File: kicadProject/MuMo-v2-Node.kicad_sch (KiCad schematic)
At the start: 76 parts, among them Q1 PJC7400, SW1 Boot0, SW2 Reset, U1 MCP73123, U2 LoRa-E5, U3 CP2102N, U4 eInk_Display_1.54"200x200px, U5 BME680, U6 TSL25911, U7 BR24G512FVT-5AE2

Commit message: V2.1
Minor update, fixing issues #2 #3 #6 #7 #8 #9 #10 #11 #12 #13 #14 #15 #16 #17 #18 and #19
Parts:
- removed R6: 470, thisProjectLibrary:0603_1608Metric, symbol Device:R
- removed SW1: Boot0, thisProjectLibrary:SW_SPST_PTS815, symbol Switch:SW_Push
- removed TP1, TP2, TP3: GND, TestPoint:TestPoint_THTPad_1.5x1.5mm_Drill0.7mm, symbol Connector:TestPoint_Probe
- removed TP5: GND, TestPoint:TestPoint_THTPad_2.5x2.5mm_Drill1.2mm, symbol Connector:TestPoint_Probe
- added C28: 4u7, thisProjectLibrary:0603_1608Metric, symbol Device:C
- added C29: 100n, thisProjectLibrary:0603_1608Metric, symbol Device:C
- added C30: 1uF/50V, thisProjectLibrary:0603_1608Metric, symbol Device:C_Small
- added JP1: Cut to disable charging, Jumper:SolderJumper-2_P1.3mm_Bridged2Bar_Pad1.0x1.5mm, symbol Jumper:SolderJumper_2_Bridged
- added U8: BR24G512FVT-5AE2, thisProjectLibrary:TSSOP-B8, symbol thisProjectLibrary:BR24G512FVT
- C15: value 1uF/50V -> 1uF/25V
- C17: value 4u7 -> 100n
- C23, C25: value 100n -> 4u7
- CONN1: value SWD -> DEBUG-SWD; footprint Connector_PinHeader_2.54mm:PinHeader_1x03_P2.54mm_Vertical -> Connector_PinHeader_2.54mm:PinHeader_1x05_P2.54mm_Vertical; symbol Connector:Conn_01x03_Male -> Connector:Conn_01x05_Male
- CONN6: value UART -> UART1
- R10, R11, R12: value 3K3 -> 5K1
- TP4, TP6: footprint TestPoint:TestPoint_THTPad_2.5x2.5mm_Drill1.2mm -> TestPoint:TestPoint_THTPad_1.5x1.5mm_Drill0.7mm
- TP7: value TestPoint_Probe -> 5V; footprint TestPoint:TestPoint_THTPad_2.5x2.5mm_Drill1.2mm -> TestPoint:TestPoint_THTPad_1.5x1.5mm_Drill0.7mm
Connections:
- net +5V: now also D4.4; no longer D4.2
- net D+: now also D4.2; no longer D4.3
- net D-: now also D4.3; no longer D4.4
- net GND: now also CONN1.2 (Pin_2), C28.2, C29.2, C30.1, U8.2 (A1), U8.3 (A3), U8.4 (GND); no longer CONN1.1 (Pin_1)
- net SWCLK: now also CONN1.4 (Pin_4); no longer CONN1.3 (Pin_3)
- net SWDIO: now also CONN1.3 (Pin_3); no longer CONN1.2 (Pin_2)
- net PREVGL: now reaches C14.2, CONN3.23 (Pin_23), D2.2 (A)
- net GATE-DRIVE: now reaches CONN3.2 (Pin_2), Q1.1 (G), R9.2
- net VSH: now reaches C10.2, CONN3.20 (Pin_20)
- net PREVGH: now reaches C13.2, CONN3.21 (Pin_21), D3.1 (K)
- net VSL: now reaches C11.2, CONN3.22 (Pin_22)
- net VCOM: now reaches C15.2, CONN3.24 (Pin_24)
- net CURRENT-SENSE: now reaches CONN3.3 (Pin_3), Q1.2 (S), R8.1
- net VGL: now reaches CONN3.4 (Pin_4)
- net VGL: now also C30.2
- net VGH: now reaches C8.2, CONN3.5 (Pin_5)
- net UART1-TX: now reaches U2.10 (PB6)
- net UART1-TX: now also CONN6.2; no longer U3.20 (RXD)
- net UART1-RX: now reaches U2.9 (PB7)
- net UART1-RX: now also CONN6.1; no longer U3.21 (TXD)
- net DISPLAY-BUSY: now reaches U2.20 (PB10)
- net DISPLAY-BUSY: now also CONN3.9 (Pin_9)
- net WRITE-PROTECT: now reaches U2.25 (PB9)
- net WRITE-PROTECT: now also R10.2, U7.7 (WP), U8.7 (WP)
- net DISPLAY-D/C: now reaches U2.26 (PB14)
- net DISPLAY-D/C: now also CONN3.11 (Pin_11)
- net SWO: now reaches U2.8 (PB3)
- net SWO: now also CONN1.5 (Pin_5)
- net +3V3 renamed +BATT
- net +BATT: now also CONN1.1 (Pin_1), C28.1, JP1.2 (B), U8.1 (A0), U8.8 (VCC); no longer C2.1, U1.3 (VBAT1), U1.4 (VBAT2)
- net BUSY: no longer names the net of U2.13 (PC0)
- net BUSY: no longer CONN3.9 (Pin_9)
- net D/C: no longer names the net of U2.12 (PC1)
- net D/C: no longer CONN3.11 (Pin_11)
- net SCK renamed SPI2-SCK
- net SCL renamed I2C2-SCL
- net I2C2-SCL: now also U8.6 (SCL)
- net SDA renamed I2C2-SDA
- net I2C2-SDA: now also U8.5 (SDA)
- net SDI renamed SPI2-MOSI
- net USART_RX renamed UART2-RX
- net UART2-RX: now also U3.21 (TXD); no longer CONN6.1
- net USART_TX renamed UART2-TX
- net UART2-TX: now also U3.20 (RXD); no longer CONN6.2
- removed net WP: R10.2, U2.23 (PA0), U7.7 (WP)
- net \RESET renamed MCU-RESET
- net MCU-RESET: now also C29.1; no longer CONN3.10 (Pin_10)
- net /CS renamed DISPLAY-CS
- new net: C2.1, JP1.1 (A), U1.3 (VBAT1), U1.4 (VBAT2)
- new net DISPLAY-RESET: CONN3.10 (Pin_10), U2.23 (PA0)
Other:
- note added: "External sensors"
- note added: "PCB Sensors"
- note removed: "Sensors"
- moved on the sheet: C1, C16, C17, C18, C19, C2, C20, C21, C22, C23, C24, C25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

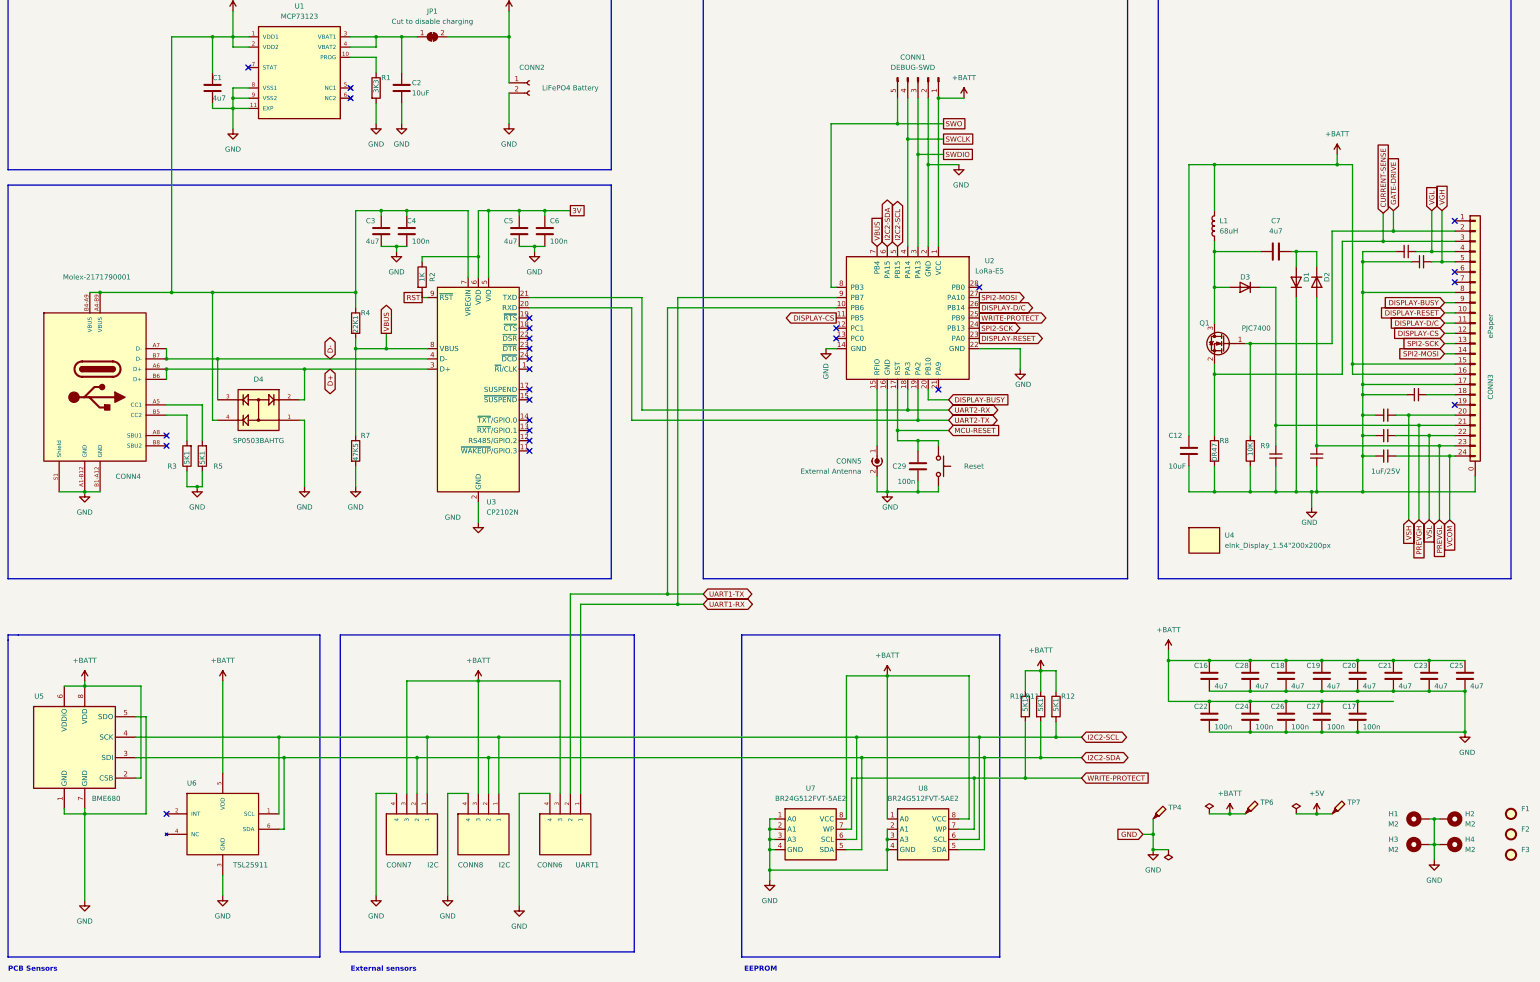
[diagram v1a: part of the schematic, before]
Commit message: cleanup references
sequential numbering for all identical parts
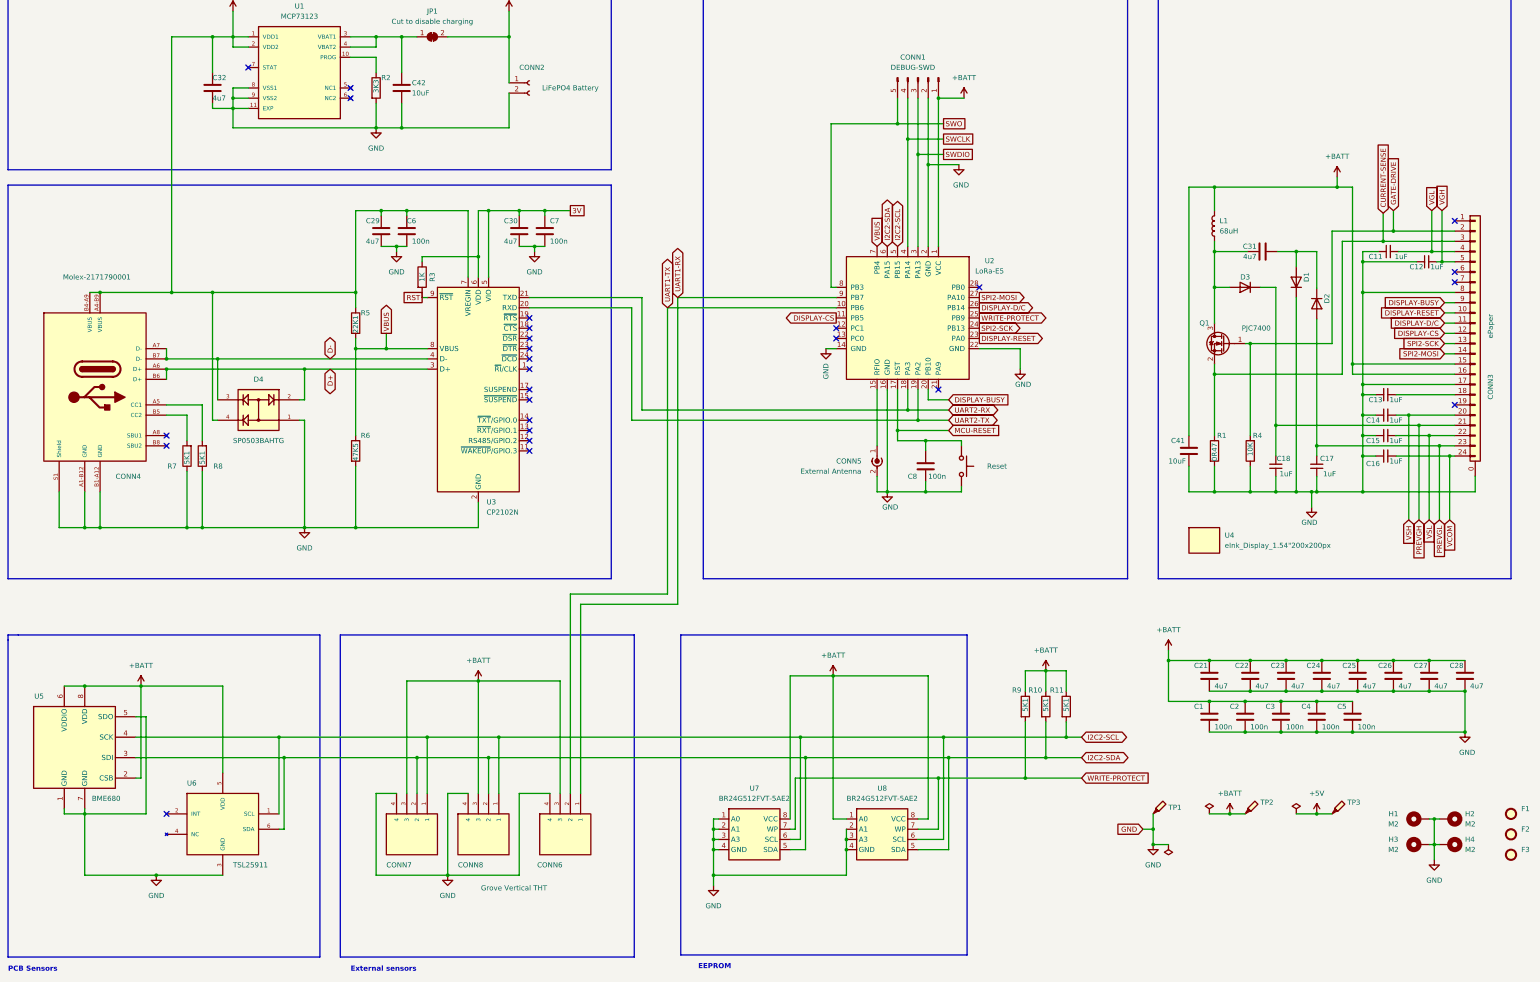
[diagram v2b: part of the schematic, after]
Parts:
- C11: renamed from C30; value 1uF/50V -> 1uF
- C12: renamed from C8; value 1uF/50V -> 1uF
- C13: renamed from C9; value 1uF/50V -> 1uF
- C14: renamed from C10; value 1uF/50V -> 1uF
- C15: renamed from C11; value 1uF/50V -> 1uF
- C16: renamed from C15; value 1uF/25V -> 1uF
- C17: renamed from C14; value 1uF/50V -> 1uF
- C18: renamed from C13; value 1uF/50V -> 1uF
- CONN6: value UART1 -> Grove Vertical THT
- CONN7, CONN8: value I2C -> Grove Vertical THT
- D1, D2: value SL03-GS08 -> SS1FL3HM3/H; supplier1PartURL https://www.mouser.be/ProductDetail/Vishay-Semiconductors/S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 -> https://www.mouser.be/ProductDetail/78-SS1FL3HM3-H; unitPrice 0.43 -> 0.38
- TP1: renamed from TP4; value GND -> testPad
- TP2: renamed from TP6; value 3V3 -> testPad
- TP3: renamed from TP7; value 5V -> testPad
- renumbered C24 to C1, C26 to C2, C16 to C21, C28 to C22, C18 to C23, C19 to C24, C20 to C25, C21 to C26, C23 to C27, C25 to C28, C3 to C29, C27 to C3, C5 to C30, C7 to C31, C1 to C32, C17 to C4, C12 to C41, C2 to C42, C22 to C5, C4 to C6, C6 to C7, C29 to C8, R8 to R1, R11 to R10, R12 to R11, R1 to R2, R2 to R3, R9 to R4, R4 to R5, R7 to R6, R3 to R7, R5 to R8, R10 to R9, SW2 to SW1
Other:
- moved on the sheet: C1, C2, C3, C31, C4, C5, C8, D2, R10, R11, TP1, U7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

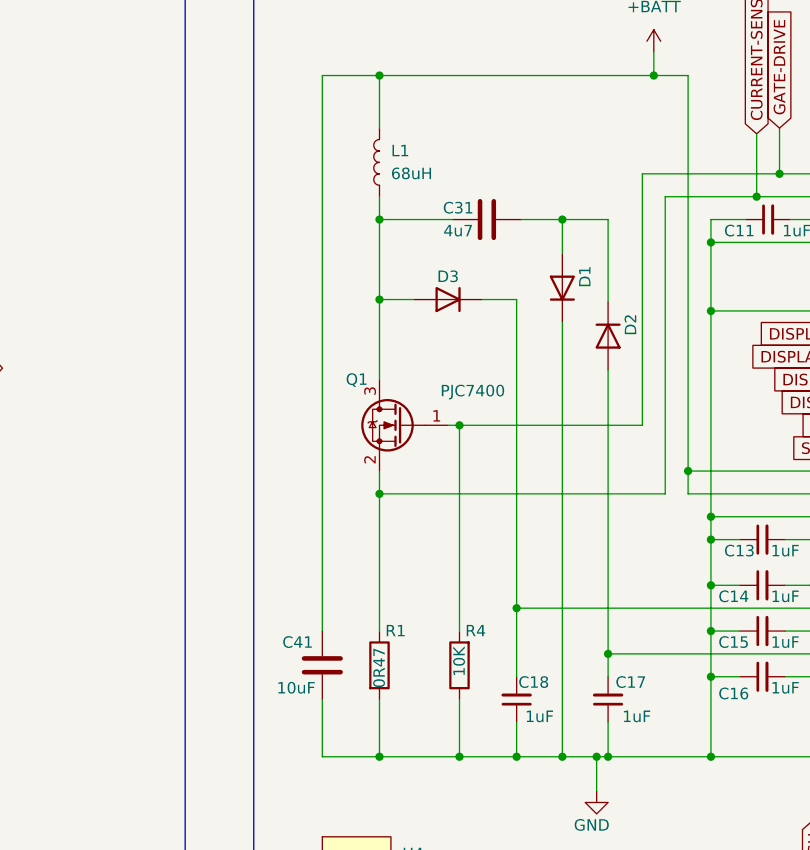
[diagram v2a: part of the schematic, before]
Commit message: Improving the BOM
Grouped designators,
Added logo to silkscreen
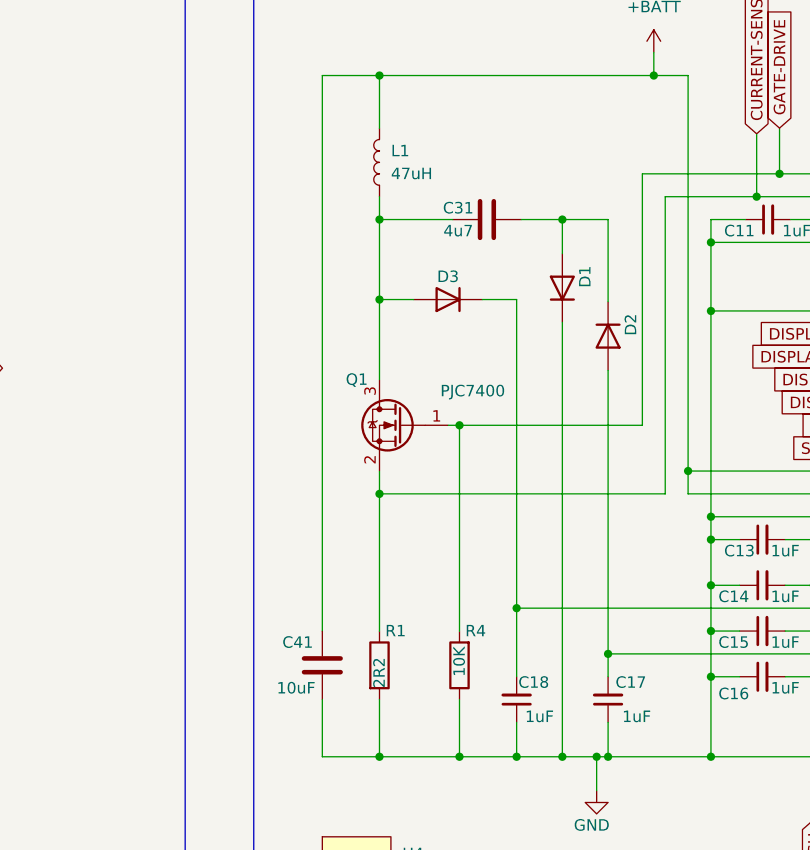
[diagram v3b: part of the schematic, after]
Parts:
- C11, C12, C13, C14, C15, C16, C17, C18: mpn C1608X5R1H105K080AB -> CGA3E1X7R1E105K080AC; supplier1PartURL https://www.mouser.be/ProductDetail/TDK/C1608X5R1H105K080AB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 -> https://www.mouser.be/ProductDetail/TDK/CGA3E1X7R1E105K080A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
- C22, C27, C28: mpn CGA3E2X7R1E104K080AA -> C1608X7S1A475K080AC; supplier1PartURL https://www.mouser.be/ProductDetail/TDK/CGA3E2X7R1E104K080A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 -> https://www.mouser.be/ProductDetail/TDK/C1608X7S1A475K080AC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
- C4, C8: mpn C1608X7S1A475K080AC -> CGA3E2X7R1E104K080AA; supplier1PartURL https://www.mouser.be/ProductDetail/TDK/C1608X7S1A475K080AC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 -> https://www.mouser.be/ProductDetail/TDK/CGA3E2X7R1E104K080A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
- CONN1: description 3-pin Header 2.54mm -> 5-pin Header 2.54mm; mpn 10129378-903001BLF -> 10129378-905002BLF; supplier1PartNumber 649-1012937890301BLF -> 649-1012937890502BLF; supplier1PartURL https://www.mouser.be/ProductDetail/Amphenol-FCI/10129378-903001BLF?qs=0lQeLiL1qybuYTJnitumiA%3D%3D -> https://www.mouser.be/ProductDetail/Amphenol-FCI/10129378-905002BLF?qs=0lQeLiL1qyZ7vSJa38rFLQ%3D%3D; unitPrice 0.1 -> 0.16
- L1: value 68uH -> 47uH; description Power Inductors - SMD 68uH -> Power Inductors - SMD 47uH; mpn VLS6045EX-680M -> VLS6045EX-470M; stock 29000 -> 50000; supplier1PartNumber 810-VLS6045EX-680M -> 810-VLS6045EX-470M; supplier1PartURL https://www.mouser.be/ProductDetail/TDK/VLS6045EX-680M?qs=o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 -> https://www.mouser.be/ProductDetail/TDK/VLS6045EX-470M?qs=o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; unitPrice 0.48 -> 0.4
- R1: value 0R47 -> 2R2; description Current Sense Resistors - SMD 0603 0.47ohm 1% Curr Sense AE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 -> Current Sense Resistors - SMD 0603 2.2ohm 5% Curr Sense AEC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; mpn ERJ-3RQFR47V -> ERJ-3RQJ2R2V; stock 160000 -> 18000; supplier1PartNumber 667-ERJ-3RQFR47V -> 667-ERJ-3RQJ2R2V; supplier1PartURL https://www.mouser.be/ProductDetail/Panasonic/ERJ-3RQFR47V?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 -> https://www.mouser.be/ProductDetail/Panasonic/ERJ-3RQJ2R2V?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; unitPrice 0.17 -> 0.1
- R10, R11, R9: mpn CR0603-JW-332ELF -> CR0603-FX-5101ELF; supplier1PartURL https://www.mouser.be/ProductDetail/Bourns/CR0603-JW-332ELF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 -> https://www.mouser.be/ProductDetail/Bourns/CR0603-FX-5101EL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

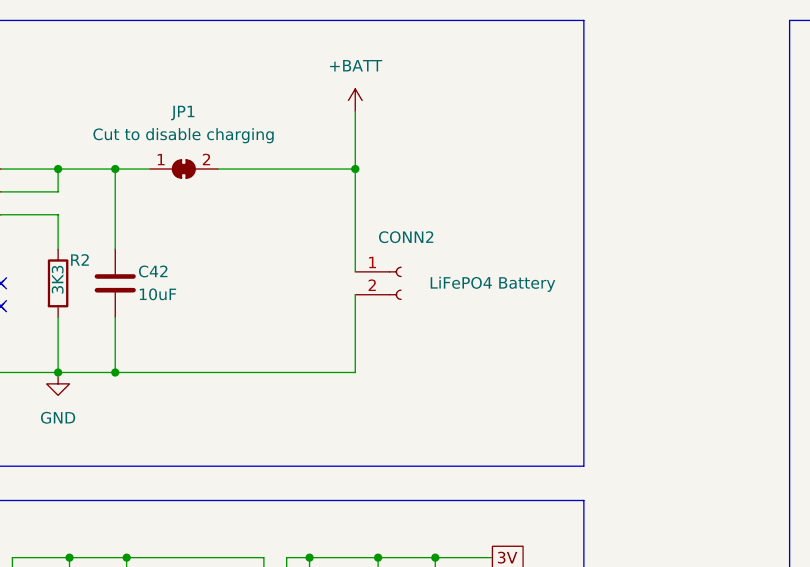
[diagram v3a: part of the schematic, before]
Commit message: corrected battery connector
To align with most common premade cables, pin 1 = GND, pin 2 - VBAT
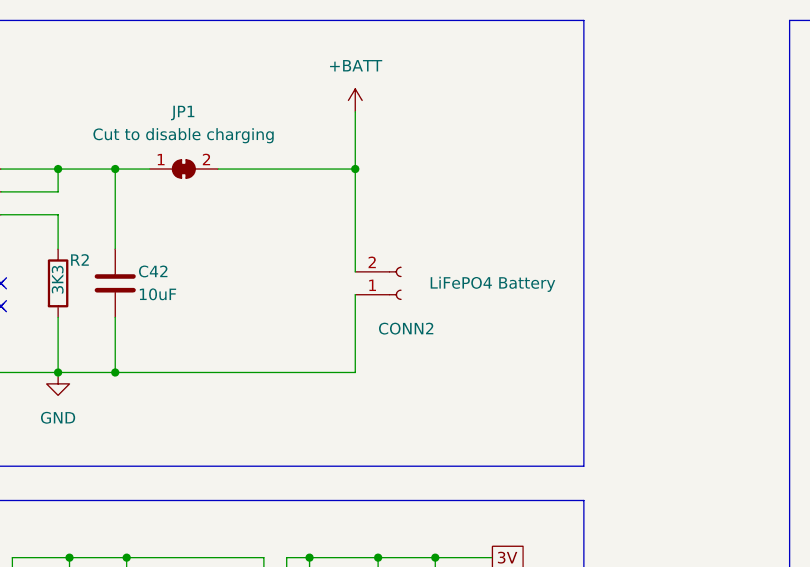
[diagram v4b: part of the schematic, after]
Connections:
- net +BATT: now also CONN2.2 (BAT-); no longer CONN2.1 (BAT+)
- net GND: now also CONN2.1 (BAT+); no longer CONN2.2 (BAT-)
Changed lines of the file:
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@@
   (title_block
     (title "MuMo-v2-Node")
-    (date "2023-02-07")
-    (rev "V2.1")
+    (date "2023-03-17")
+    (rev "V2.2")
     (company "Universiteit Antwerpen")
     (comment 1 "pascal.roobrouck@gmail.com")
@@
     (pin "1")
   )
-  (symbol (lib_id "Connector:Conn_01x02_Female") (at 154.94 52.07 0) (unit 1)
+  (symbol (lib_id "Connector:Conn_01x02_Female") (at 154.94 54.61 0) (mirror x) (unit 1)
     (in_bom yes) (on_board yes)
-    (property "Reference" "CONN2" (id 0) (at 152.4 48.26 0)
+    (property "Reference" "CONN2" (id 0) (at 152.4 58.42 0)
       (effects (font (size 1.27 1.27)) (justify left))
     )
-    (property "Value" "B2B-XH-A (LF)(SN)" (id 1) (at 153.67 58.42 0)
+    (property "Value" "B2B-XH-A (LF)(SN)" (id 1) (at 153.67 48.26 0)
       (effects (font (size 1.27 1.27)) (justify left) hide)
     )
-    (property "Footprint" "Connector_JST:JST_XH_B2B-XH-A_1x02_P2.50mm_Vertical" (id 2) (at 154.94 41.91 0)
+    (property "Footprint" "Connector_JST:JST_XH_B2B-XH-A_1x02_P2.50mm_Vertical" (id 2) (at 154.94 64.77 0)
       (effects (font (size 1.27 1.27)) hide)
     )
-    (property "Datasheet" "https://www.farnell.com/datasheets/2057209.pdf" (id 3) (at 154.94 44.45 0)
+    (property "Datasheet" "https://www.farnell.com/datasheets/2057209.pdf" (id 3) (at 154.94 62.23 0)
       (effects (font (size 1.27 1.27)) hide)
     )
-    (property "MANUFACTURER" "" (id 4) (at 156.21 38.1 0)
+    (property "MANUFACTURER" "" (id 4) (at 156.21 68.58 0)
       (effects (font (size 1.27 1.27)) hide)
     )
-    (property "supplier1Name" "Farnell" (id 5) (at 156.21 35.56 0)
+    (property "supplier1Name" "Farnell" (id 5) (at 156.21 71.12 0)
       (effects (font (size 1.27 1.27)) hide)
     )
-    (property "supplier1PartURL" "https://be.farnell.com/jst-japan-solderless-terminals/b2b-xh-a-lf-sn/header-vertical-2way/dp/1516276" (id 6) (at 154.94 46.99 0)
+    (property "supplier1PartURL" "https://be.farnell.com/jst-japan-solderless-terminals/b2b-xh-a-lf-sn/header-vertical-2way/dp/1516276" (id 6) (at 154.94 59.69 0)
       (effects (font (size 1.27 1.27)) hide)
     )
-    (property "manufacturer" "JST" (id 7) (at 154.94 52.07 0)
+    (property "manufacturer" "JST" (id 7) (at 154.94 54.61 0)
       (effects (font (size 1.27 1.27)) hide)
     )
-    (property "mpn" "B2B-XH-A (LF)(SN)" (id 8) (at 154.94 52.07 0)
+    (property "mpn" "B2B-XH-A (LF)(SN)" (id 8) (at 154.94 54.61 0)
       (effects (font (size 1.27 1.27)) hide)
     )
-    (property "stock" "1500000" (id 9) (at 154.94 52.07 0)
+    (property "stock" "1500000" (id 9) (at 154.94 54.61 0)
       (effects (font (size 1.27 1.27)) hide)
     )
-    (property "supplier1PartNumber" "1516276" (id 10) (at 154.94 52.07 0)
+    (property "supplier1PartNumber" "1516276" (id 10) (at 154.94 54.61 0)
       (effects (font (size 1.27 1.27)) hide)
     )
-    (property "unitPrice" "0.09" (id 11) (at 154.94 52.07 0)
+    (property "unitPrice" "0.09" (id 11) (at 154.94 54.61 0)
       (effects (font (size 1.27 1.27)) hide)
     )
-    (property "description" "JST XH 2pin THT Vertical" (id 12) (at 154.94 52.07 0)
+    (property "description" "JST XH 2pin THT Vertical" (id 12) (at 154.94 54.61 0)
       (effects (font (size 1.27 1.27)) hide)
     )
-    (property "supplier2Name" "Digi-Key" (id 13) (at 154.94 52.07 0)
+    (property "supplier2Name" "Digi-Key" (id 13) (at 154.94 54.61 0)
       (effects (font (size 1.27 1.27)) hide)
     )
-    (property "supplier2PartNumber" "455-2247-ND" (id 14) (at 154.94 52.07 0)
+    (property "supplier2PartNumber" "455-2247-ND" (id 14) (at 154.94 54.61 0)
       (effects (font (size 1.27 1.27)) hide)
     )
-    (property "supplier2PartURL" "https://www.digikey.be/nl/products/detail/jst-sales-america-inc/B2B-XH-A-LF-SN/1651045" (id 15) (at 154.94 52.07 0)
+    (property "supplier2PartURL" "https://www.digikey.be/nl/products/detail/jst-sales-america-inc/B2B-XH-A-LF-SN/1651045" (id 15) (at 154.94 54.61 0)
       (effects (font (size 1.27 1.27)) hide)
     )
